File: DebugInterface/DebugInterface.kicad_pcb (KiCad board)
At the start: 2 copper layers, 157 x 175.6 mm, 62 parts, among them J1 IDC-16M, J10 IDC-16M, J11 IDC-16M, J12 IDC-16M, J13 IDC-16M, J14 IDC-16M, J15 IDC-16M, J16 IDC-16M, J17 IDC-16M, J18 IDC-16M, J19 IDC-16M, J2 IDC-16M, J20 IDC-16M, J21 IDC-16M, J22 IDC-16M, J23 IDC-16M, J24 IDC-16M, J25 USB_B, J26 ISP, J27 Barrel_Jack_MountingPin, J3 IDC-16M, J4 IDC-16M, J5 IDC-16M, J6 IDC-16M, J7 IDC-16M, J8 IDC-16M, J9 IDC-16M, U1 8255, U10 PIC18F2550-ISO, U2 8255, U3 8255, U4 8255, U5 8255, U6 8255, U7 8255, U8 8255, U9 74LS138, Y1 20MHz

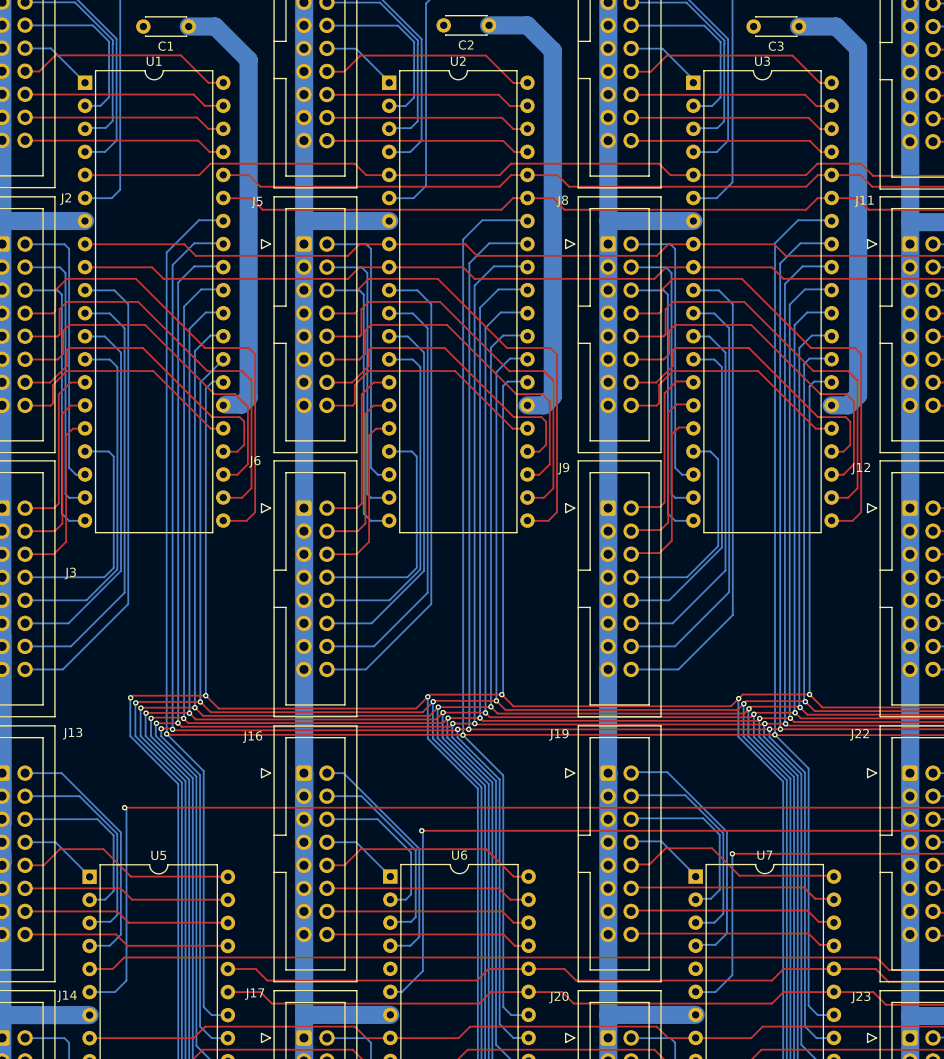
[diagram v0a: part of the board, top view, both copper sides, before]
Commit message: DebugInterface: Last-minute corrections
Spotted unconnected Rd line
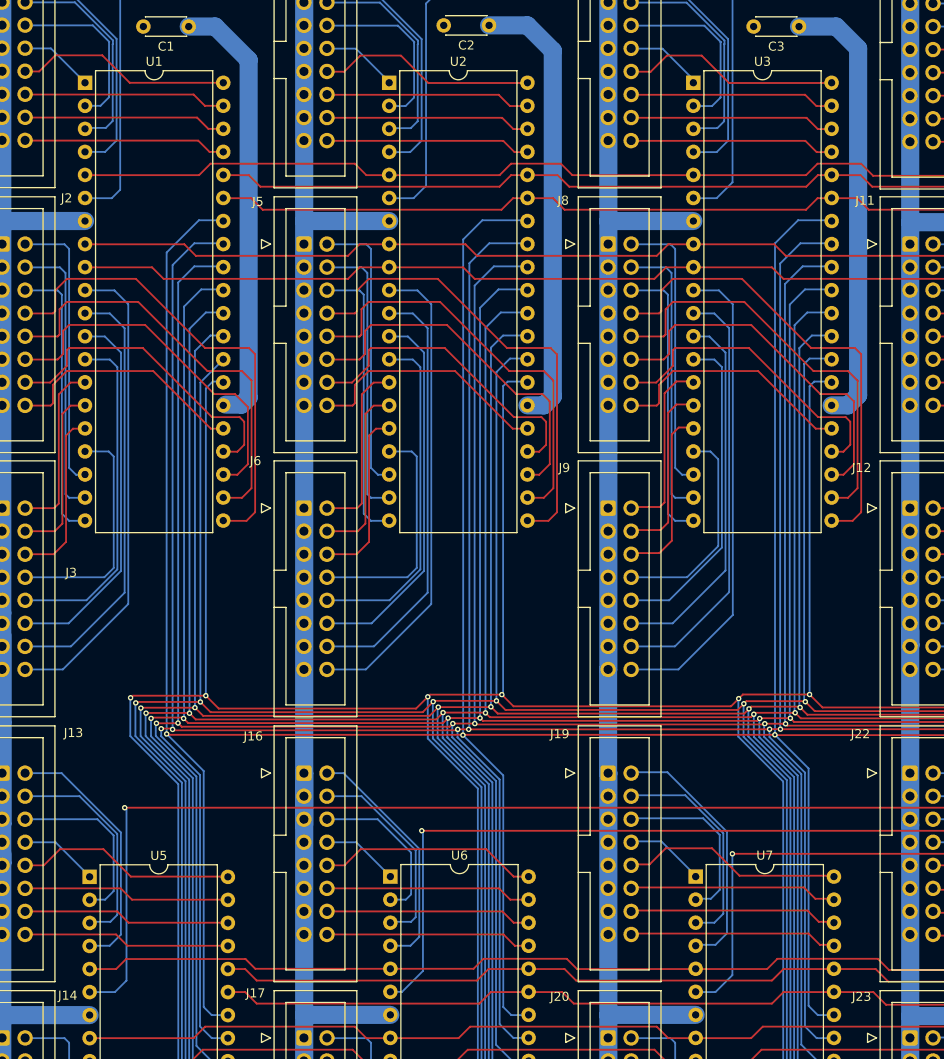
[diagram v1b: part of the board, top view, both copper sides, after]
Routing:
- net /~{RD}: track 367.5 -> 369.2 mm

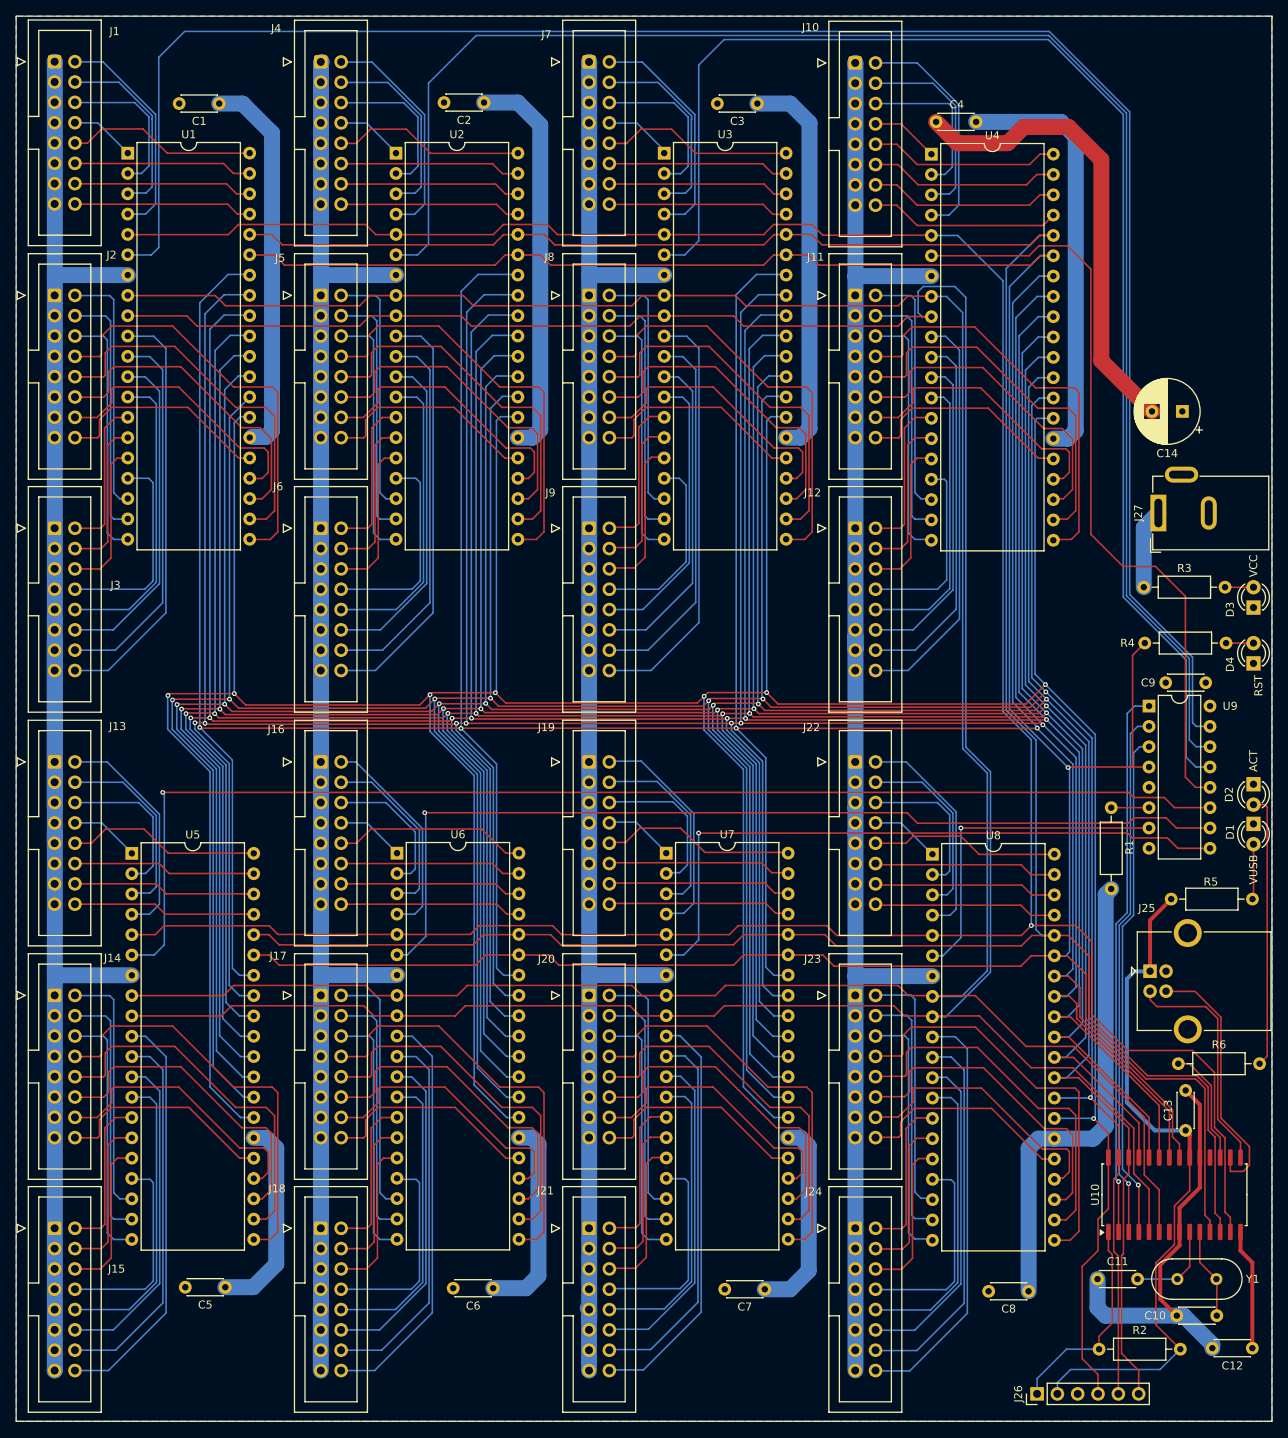
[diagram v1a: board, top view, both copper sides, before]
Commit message: DebugInterface: Port designators on silk screen
For more convenience
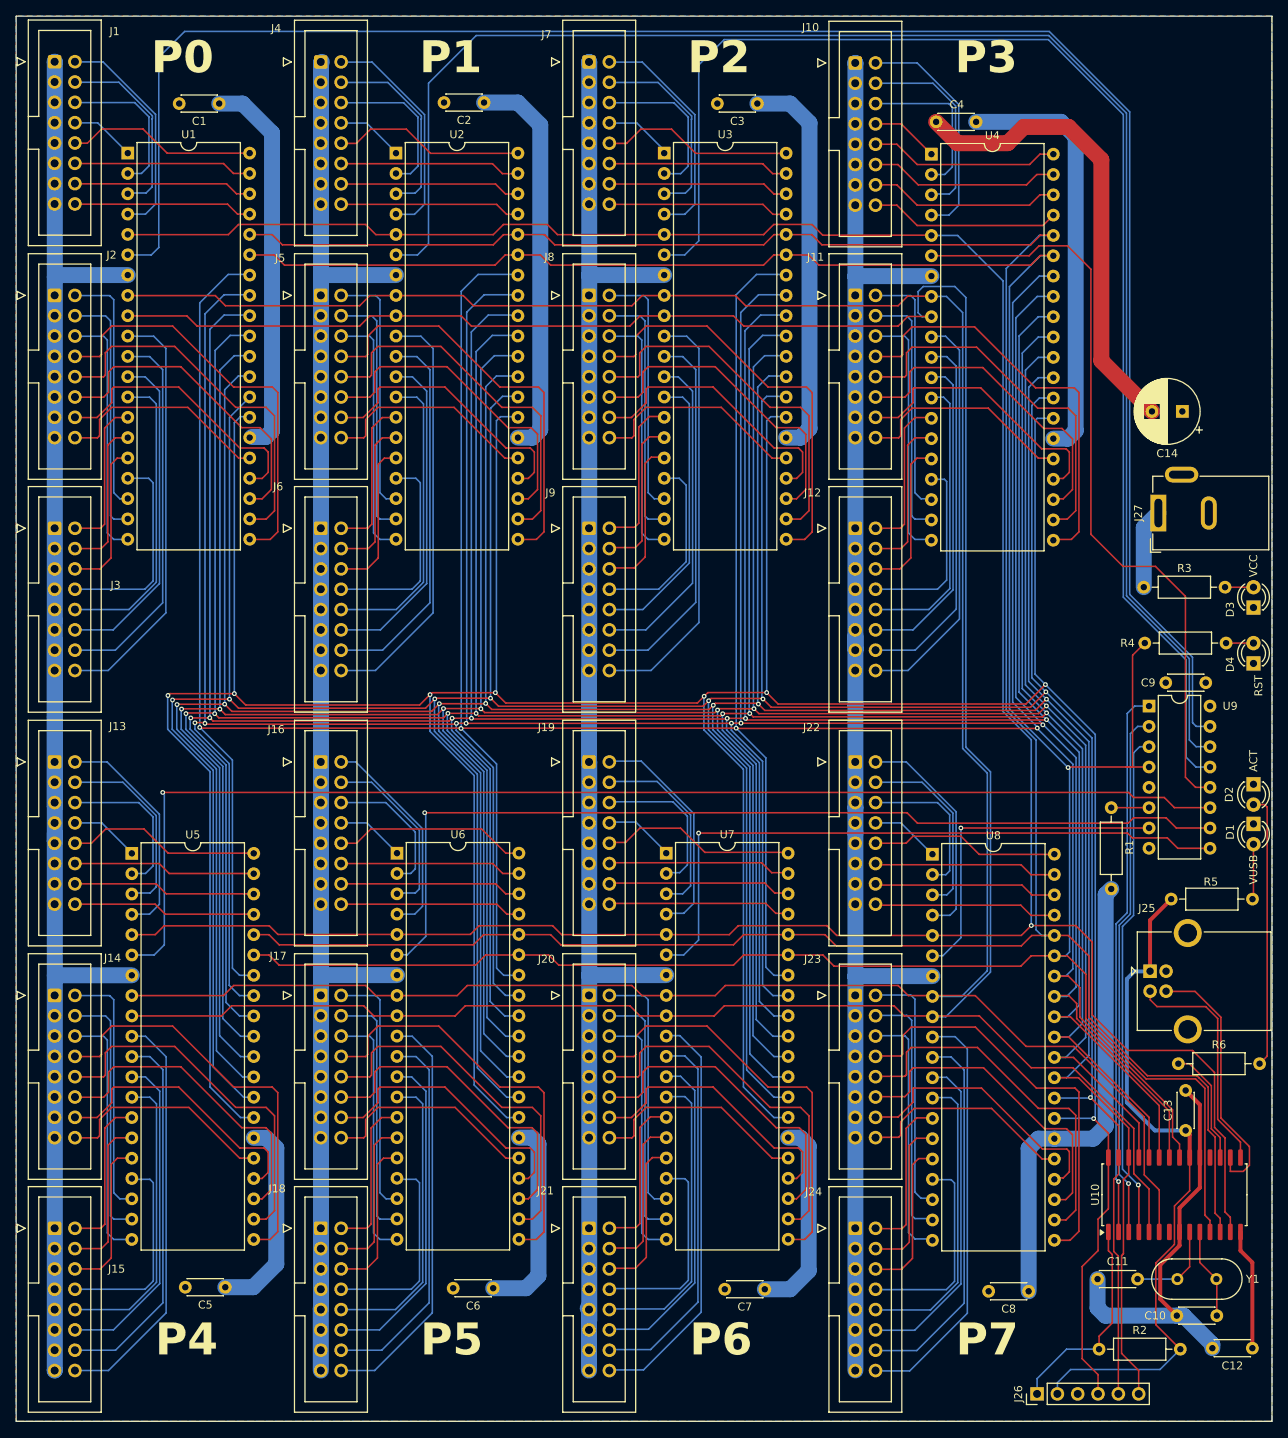
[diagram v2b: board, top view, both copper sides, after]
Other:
- board text added: "P0"
- board text added: "P1"
- board text added: "P2"
- board text added: "P3"
- board text added: "P4"
- board text added: "P5"
- board text added: "P6"
- board text added: "P7"
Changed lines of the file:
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@@
 		(layer "Edge.Cuts")
+	)
+	(gr_text "P4"
+		(at 32.384238 185.42 0)
+		(layer "F.SilkS")
+		(effects
+			(font
+				(size 4 4)
+				(thickness 0.8)
+				(bold yes)
+			)
+			(justify left bottom)
+		)
+	)
+	(gr_text "P5"
+		(at 65.531238 185.42 0)
+		(layer "F.SilkS")
+		(effects
+			(font
+				(size 4 4)
+				(thickness 0.8)
+				(bold yes)
+			)
+			(justify left bottom)
+		)
+	)
+	(gr_text "P1"
+		(at 65.405 25.146 0)
+		(layer "F.SilkS")
+		(effects
+			(font
+				(size 4 4)
+				(thickness 0.8)
+				(bold yes)
+			)
+			(justify left bottom)
+		)
+	)
+	(gr_text "P0"
+		(at 31.877 25.146 0)
+		(layer "F.SilkS")
+		(effects
+			(font
+				(size 4 4)
+				(thickness 0.8)
+				(bold yes)
+			)
+			(justify left bottom)
+		)
+	)
+	(gr_text "P7"
+		(at 132.460238 185.42 0)
+		(layer "F.SilkS")
+		(effects
+			(font
+				(size 4 4)
+				(thickness 0.8)
+				(bold yes)
+			)
+			(justify left bottom)
+		)
+	)
+	(gr_text "P6"
+		(at 99.186238 185.42 0)
+		(layer "F.SilkS")
+		(effects
+			(font
+				(size 4 4)
+				(thickness 0.8)
+				(bold yes)
+			)
+			(justify left bottom)
+		)
+	)
+	(gr_text "P2"
+		(at 98.933 25.146 0)
+		(layer "F.SilkS")
+		(effects
+			(font
+				(size 4 4)
+				(thickness 0.8)
+				(bold yes)
+			)
+			(justify left bottom)
+		)
+	)
+	(gr_text "P3"
+		(at 132.334 25.146 0)
+		(layer "F.SilkS")
+		(effects
+			(font
+				(size 4 4)
+				(thickness 0.8)
+				(bold yes)
+			)
+			(justify left bottom)
+		)
 	)
 	(segment
